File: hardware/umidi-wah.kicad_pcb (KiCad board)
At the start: 2 copper layers, 128 x 101 mm, 92 parts, among them J1 Power, J10 Midi_thru, J11 Midi_t/o, J12 Midi_out, J2 Pots Main, J3 Pots Front, J4 Switch, J5 Input, J6 Output, J7 Conn_02x05_Odd_Even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

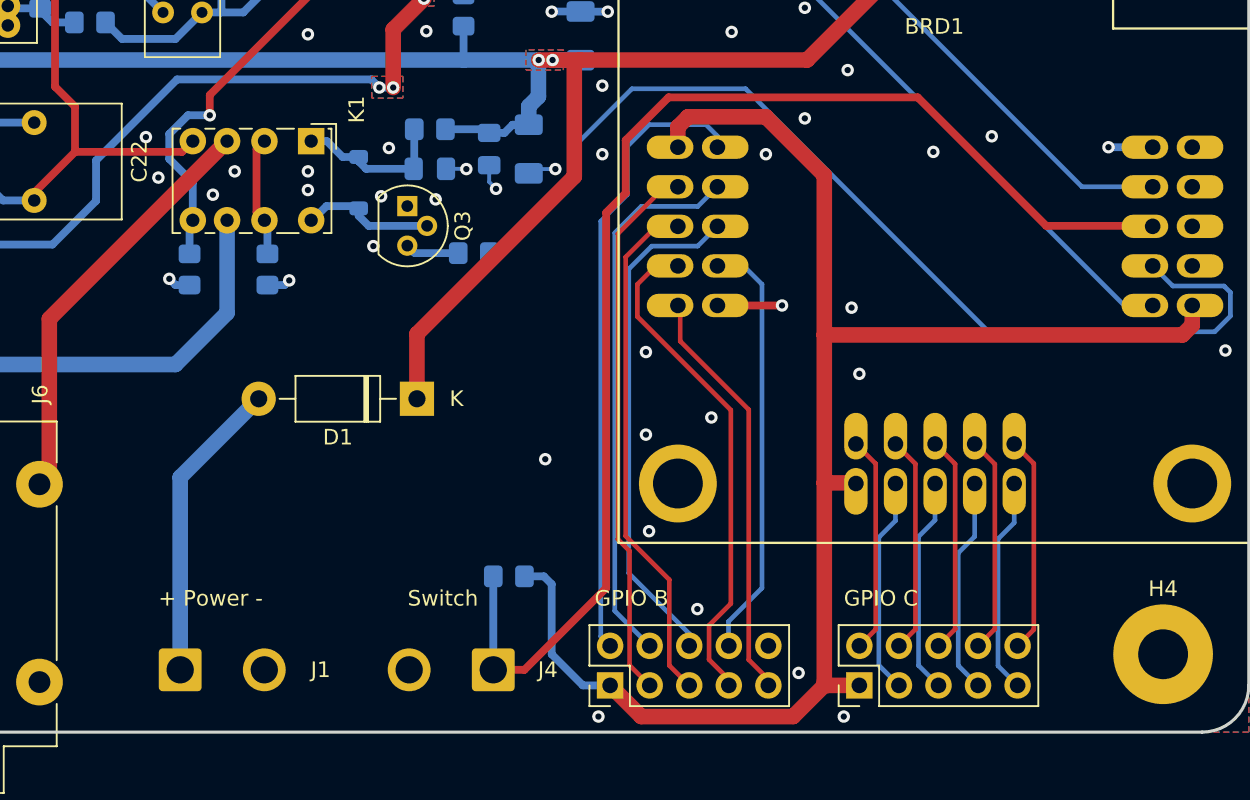
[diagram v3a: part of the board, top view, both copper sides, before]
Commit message: Rotate pwr connector (increase clearance to signal out)
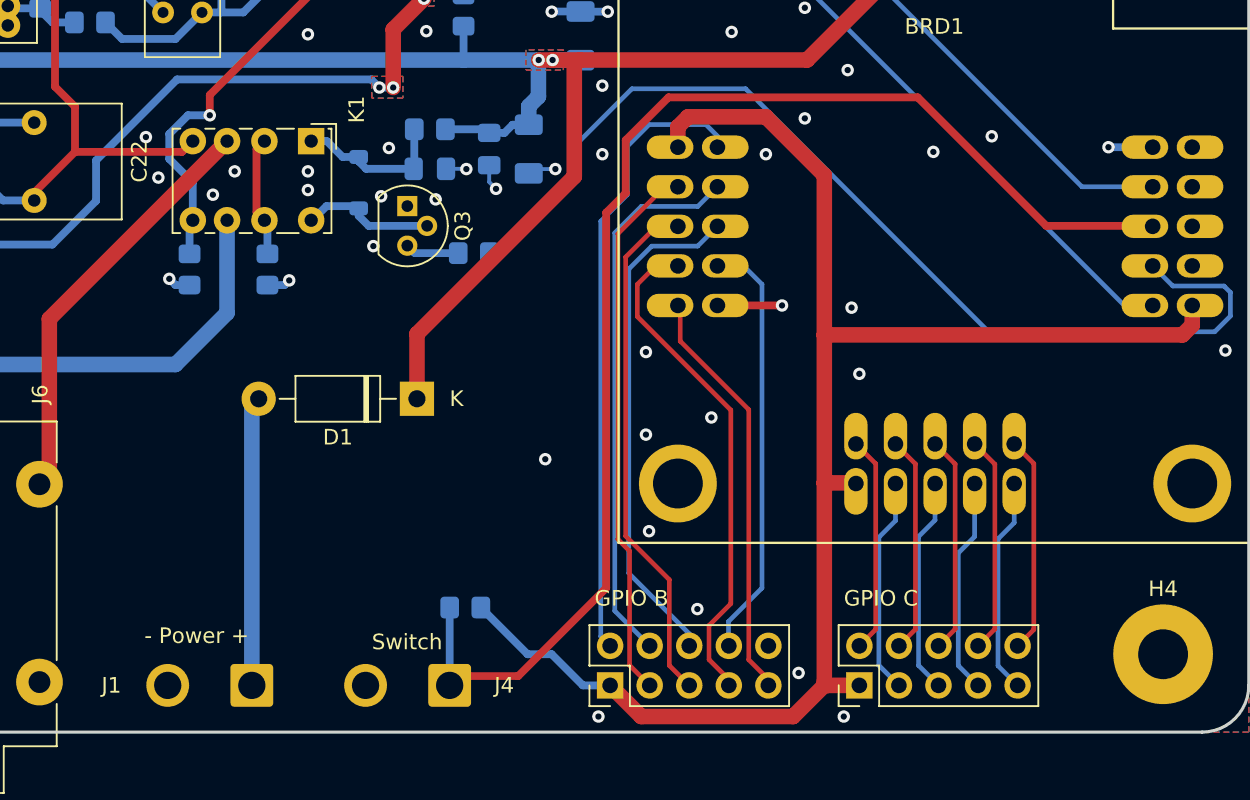
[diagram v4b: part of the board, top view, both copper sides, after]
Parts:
- moved J1 4.71 mm to (127.0, 134.0), turned to 180 degrees
- moved R25 3.44 mm to (140.7, 129.0)
- moved J4 2.97 mm to (139.7, 134.0)
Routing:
- net /toggle_switch: track 81.9 -> 85.3 mm
- net Net-(D1-A): track 19.5 -> 18.6 mm
- net /umidi_3v3: track 101.3 -> 100.6 mm
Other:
- board text added: "- Power +"
- board text added: "- pwr +"
- board text removed: "+ Power -"
- board text removed: "+ pwr -"
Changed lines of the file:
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@@
 	(footprint "Connector_Wire:SolderWire-1sqmm_1x02_P5.4mm_D1.4mm_OD2.7mm"
 		(layer "F.Cu")
-		(at 122.4 133)
+		(at 127 134 180)
 		(descr "Soldered wire connection, for 2 times 1 mm² wires, basic insulation, conductor diameter 1.4mm, outer diameter 2.7mm, size source Multi-Contact FLEXI-E 1.0 (https://ec.staubli.com/AcroFiles/Catalogues/TM_Cab-Main-11014119_(en)_hi.pdf), bend radius 3 times outer diameter, generated with kicad-footprint-generator")
 		(tags "connector wire 1sqmm")
 		(property "Reference" "J1"
-			(at 9.017 0 0)
+			(at 9.017 0 180)
 			(layer "F.SilkS")
 			(effects
@@
 		)
 		(property "Value" "Power"
-			(at 10.795 0 0)
+			(at 10.795 0 180)
 			(layer "F.Fab")
 			(effects
@@
 		)
 		(property "Footprint" ""
-			(at 0 0 0)
+			(at 0 0 180)
 			(unlocked yes)
 			(layer "F.Fab")
@@
 		)
 		(property "Datasheet" ""
-			(at 0 0 0)
+			(at 0 0 180)
 			(unlocked yes)
 			(layer "F.Fab")
@@
 		)
 		(property "Description" "Generic connector, single row, 01x02, script generated (kicad-library-utils/schlib/autogen/connector/)"
-			(at 0 0 0)
+			(at 0 0 180)
 			(unlocked yes)
 			(layer "F.Fab")
@@
 		)
 		(property "Supplier Link" ""
-			(at 0 0 0)
+			(at 0 0 180)
 			(layer "F.Fab")
 			(hide yes)
@@
 		(attr exclude_from_pos_files)
 		(fp_line
-			(start -2.1 -1.88)
-			(end -2.1 1.88)
+			(start 7.5 1.88)
+			(end 7.5 -1.88)
 			(stroke
 				(width 0.05)
@@
 		)
 		(fp_line
-			(start -2.1 1.88)
-			(end 2.1 1.88)
+			(start 7.5 -1.88)
+			(end 3.3 -1.88)
 			(stroke
 				(width 0.05)
@@
 		)
 		(fp_line
-			(start 2.1 -1.88)
-			(end -2.1 -1.88)
+			(start 3.3 1.88)
+			(end 7.5 1.88)
 			(stroke
 				(width 0.05)
@@
 		)
 		(fp_line
-			(start 2.1 1.88)
-			(end 2.1 -1.88)
+			(start 3.3 -1.88)
+			(end 3.3 1.88)
 			(stroke
 				(width 0.05)
@@
 		)
 		(fp_line
-			(start 3.3 -1.88)
-			(end 3.3 1.88)
+			(start 2.1 1.88)
+			(end 2.1 -1.88)
 			(stroke
 				(width 0.05)
@@
 		)
 		(fp_line
-			(start 3.3 1.88)
-			(end 7.5 1.88)
+			(start 2.1 -1.88)
+			(end -2.1 -1.88)
 			(stroke
 				(width 0.05)
@@
 		)
 		(fp_line
-			(start 7.5 -1.88)
-			(end 3.3 -1.88)
+			(start -2.1 1.88)
+			(end 2.1 1.88)
 			(stroke
 				(width 0.05)
@@
 		)
 		(fp_line
-			(start 7.5 1.88)
-			(end 7.5 -1.88)
+			(start -2.1 -1.88)
+			(end -2.1 1.88)
 			(stroke
 				(width 0.05)
@@
 		)
 		(fp_circle
-			(center 0 0)
-			(end 1.35 0)
+			(center 5.4 0)
+			(end 6.75 0)
 			(stroke
 				(width 0.1)
@@
 		)
 		(fp_circle
-			(center 5.4 0)
-			(end 6.75 0)
+			(center 0 0)
+			(end 1.35 0)
 			(stroke
 				(width 0.1)
@@
 		)
 		(fp_text user "${REFERENCE}"
-			(at 2.7 0 90)
+			(at 2.7 0 270)
 			(layer "F.Fab")
 			(effects
@@
 		)
 		(pad "1" thru_hole roundrect
-			(at 0 0)
+			(at 0 0 180)
 			(size 2.75 2.75)
 			(drill 1.75)
@@
 		)
 		(pad "2" thru_hole circle
-			(at 5.4 0)
+			(at 5.4 0 180)
 			(size 2.75 2.75)
 			(drill 1.75)
@@
 	(footprint "Connector_Wire:SolderWire-1sqmm_1x02_P5.4mm_D1.4mm_OD2.7mm"
 		(layer "F.Cu")
-		(at 142.5 133 180)
+		(at 139.7 134 180)
 		(descr "Soldered wire connection, for 2 times 1 mm² wires, basic insulation, conductor diameter 1.4mm, outer diameter 2.7mm, size source Multi-Contact FLEXI-E 1.0 (https://ec.staubli.com/AcroFiles/Catalogues/TM_Cab-Main-11014119_(en)_hi.pdf), bend radius 3 times outer diameter, generated with kicad-footprint-generator")
 		(tags "connector wire 1sqmm")
@@
 	(footprint "Resistor_SMD:R_0805_2012Metric_Pad1.20x1.40mm_HandSolder"
 		(layer "B.Cu")
-		(at 143.5 127)
+		(at 140.7 129)
 		(descr "Resistor SMD 0805 (2012 Metric), square (rectangular) end terminal, IPC_7351 nominal with elongated pad for handsoldering. (Body size source: IPC-SM-782 page 72, https://www.pcb-3d.com/wordpress/wp-content/uploads/ipc-sm-782a_amendment_1_and_2.pdf), generated with kicad-footprint-generator")
 		(tags "resistor handsolder")
@@
 		)
 	)
-	(gr_text "+ Power -"
-		(at 121 129 0)
+	(gr_text "- Power +"
+		(at 120.1 131.4 0)
 		(layer "F.SilkS")
 		(effects
@@
 	)
 	(gr_text "Switch"
-		(at 137 129 0)
+		(at 134.7 131.8 0)
 		(layer "F.SilkS")
 		(effects
@@
 	)
 	(gr_text "sw"
-		(at 138 128 0)
+		(at 135.5 131 0)
 		(layer "F.Mask")
 		(effects
 			(font
-				(size 1.5 1.5)
+				(size 1.2 1.2)
 				(thickness 0.3)
 				(bold yes)
@@
 		)
 	)
-	(gr_text "+ pwr -"
-		(at 120 128 0)
+	(gr_text "- pwr +"
+		(at 120.15779 131 0)
 		(layer "F.Mask")
 		(effects
 			(font
-				(size 1.5 1.5)
+				(size 1.2 1.2)
 				(thickness 0.3)
 				(bold yes)
@@
 	)
 	(segment
-		(start 122.4 120.64)
-		(end 127.44 115.6)
+		(start 127 134)
+		(end 127 116.04)
 		(width 1)
 		(layer "B.Cu")
@@
 	)
 	(segment
-		(start 122.4 133)
-		(end 122.4 120.64)
+		(start 127 116.04)
+		(end 127.44 115.6)
 		(width 1)
 		(layer "B.Cu")
@@
 	)
 	(segment
-		(start 146.25 127.5)
+		(start 144.7 132)
 		(end 146.25 132)
 		(width 0.5)
@@
 	)
 	(segment
-		(start 148.25 134)
-		(end 150 134)
-		(width 0.5)
-		(layer "B.Cu")
-		(net 25)
-	)
-	(segment
-		(start 144.5 127)
-		(end 145.75 127)
+		(start 146.25 132)
+		(end 148.25 134)
 		(width 0.5)
 		(layer "B.Cu")
@@
 	)
 	(segment
-		(start 146.25 132)
-		(end 148.25 134)
+		(start 148.25 134)
+		(end 150 134)
 		(width 0.5)
 		(layer "B.Cu")
@@
 	)
 	(segment
-		(start 145.75 127)
-		(end 146.25 127.5)
+		(start 141.7 129)
+		(end 144.7 132)
 		(width 0.5)
 		(layer "B.Cu")
@@
 	)
 	(segment
-		(start 153.75 96.25)
-		(end 169.75 96.25)
+		(start 151 102.4)
+		(end 149.75 103.65)
 		(width 0.5)
 		(layer "F.Cu")
@@
 	)
 	(segment
-		(start 178 104.5)
-		(end 184.8 104.5)
+		(start 169.75 96.25)
+		(end 153.75 96.25)
 		(width 0.5)
 		(layer "F.Cu")
@@
 	)
 	(segment
-		(start 149.75 127.75)
-		(end 149.75 103.65)
+		(start 184.8 104.5)
+		(end 178 104.5)
 		(width 0.5)
 		(layer "F.Cu")
@@
 	)
 	(segment
-		(start 144.5 133)
-		(end 149.75 127.75)
+		(start 151 99)
+		(end 151 102.4)
 		(width 0.5)
 		(layer "F.Cu")
@@
 	)
 	(segment
-		(start 169.75 96.25)
-		(end 178 104.5)
+		(start 144.1 133.4)
+		(end 140.3 133.4)
 		(width 0.5)
 		(layer "F.Cu")
@@
 	)
 	(segment
-		(start 149.75 103.65)
-		(end 151 102.4)
+		(start 178 104.5)
+		(end 169.75 96.25)
 		(width 0.5)
 		(layer "F.Cu")
@@
 	)
 	(segment
-		(start 151 99)
-		(end 153.75 96.25)
+		(start 140.3 133.4)
+		(end 139.7 134)
 		(width 0.5)
 		(layer "F.Cu")
@@
 	)
 	(segment
-		(start 151 102.4)
+		(start 153.75 96.25)
 		(end 151 99)
 		(width 0.5)
@@
 	)
 	(segment
-		(start 143.7 133)
-		(end 144.5 133)
+		(start 149.75 103.65)
+		(end 149.75 127.75)
+		(width 0.5)
+		(layer "F.Cu")
+		(net 28)
+	)
+	(segment
+		(start 149.75 127.75)
+		(end 144.1 133.4)
 		(width 0.5)
 		(layer "F.Cu")
@@
 	)
 	(segment
-		(start 142.5 127)
-		(end 142.5 133)
+		(start 139.7 129)
+		(end 139.7 134)
 		(width 0.5)
 		(layer "B.Cu")

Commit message: Replace gpio connectors by boxed headers
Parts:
- J7, J8: footprint Connector_PinHeader_2.54mm:PinHeader_2x05_P2.54mm_Vertical -> Connector_IDC:IDC-Header_2x05_P2.54mm_Vertical
- moved J4 14.1 mm to (129.4, 124.2)
- moved R25 7.23 mm to (135.2, 124.2)
- moved J7 7.07 mm to (143.0, 133.0)
- moved J1 3.00 mm to (130.0, 134.0)
- moved J8 1.41 mm to (165.0, 133.0)
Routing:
- net /umidi_3v3: track 100.6 -> 108.3 mm
- net Net-(BRD1B-PA6(ADC6)): track 27.5 -> 31.2 mm
- net Net-(BRD1B-PA5(ADC5)): track 32.4 -> 35.0 mm
- net Net-(BRD1B-PA7(ADC7)): track 26.8 -> 28.6 mm
- net Net-(BRD1B-PA3(ADC3)): track 33.4 -> 31.9 mm
- net Net-(D1-A): track 18.6 -> 20.0 mm
- net Net-(BRD1B-PA0(ADC0)): track 40.4 -> 41.8 mm
- net Net-(BRD1B-PA4(ADC4)): track 32.6 -> 31.3 mm
- net /toggle_switch: track 85.3 -> 84.2 mm, vias 0 -> 1
- net Net-(BRD1C-PB1): track 13.9 -> 13.3 mm
- net Net-(BRD1C-PC1(SCL)): track 13.9 -> 13.3 mm
- net Net-(BRD1C-PB3(DACB::DAC1)): track 13.9 -> 13.3 mm
- net Net-(BRD1C-PB2(DACB::DAC0)): track 13.9 -> 13.3 mm
- net Net-(BRD1C-PC3(C0::TXD0)): track 13.9 -> 13.3 mm
- net Net-(BRD1C-PC2(C0::RXD0)): track 13.9 -> 13.4 mm
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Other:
- board text added: "gpio1"
- board text added: "gpio2"
- board text removed: "- Power +"
- board text removed: "Switch"

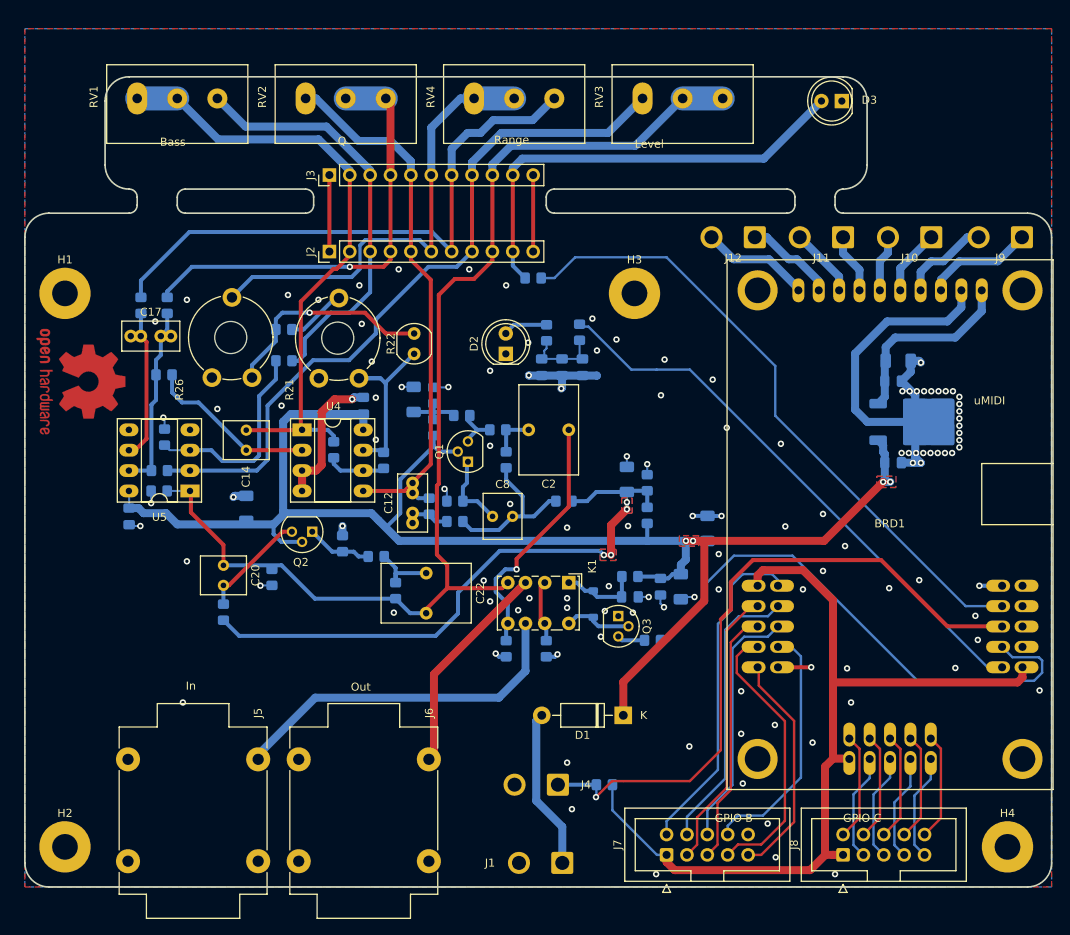
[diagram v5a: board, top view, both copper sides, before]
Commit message: Small tweaks -> DRC clean
Fix typo in board name, move umidi slighty south
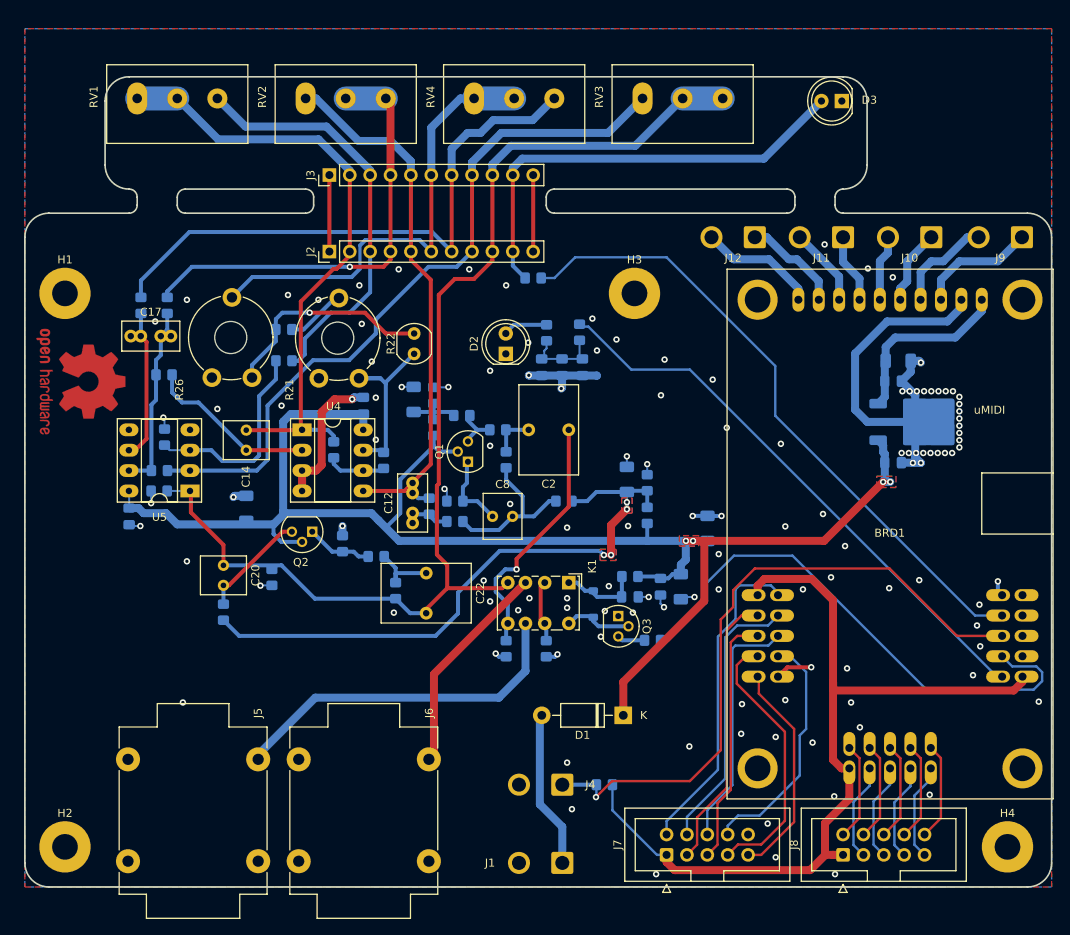
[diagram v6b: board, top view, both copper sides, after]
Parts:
- moved BRD1 1.17 mm to (170.9, 93.0)
- moved J4 0.55 mm to (130.0, 124.2)
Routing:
- net GND: track 147.4 -> 144.7 mm, vias 118 -> 125
- net Net-(BRD1B-PA0(ADC0)): track 41.8 -> 40.3 mm
- net Net-(BRD1C-PC2(C0::RXD0)): track 13.4 -> 12.2 mm
- net Net-(BRD1C-PB2(DACB::DAC0)): track 13.3 -> 12.2 mm
- net Net-(BRD1C-PB0): track 13.3 -> 12.2 mm
- net Net-(BRD1B-PA7(ADC7)): track 28.6 -> 27.4 mm
- net Net-(BRD1A-MIDI_thru+): track 8.22 -> 9.39 mm
- net Net-(BRD1A-MIDI_out-): track 13.7 -> 14.9 mm
- net Net-(BRD1A-MIDI_out+): track 11.4 -> 12.6 mm
- net Net-(BRD1A-MIDI_in-): track 11.3 -> 12.5 mm
- net Net-(BRD1A-MIDI_in+): track 13.6 -> 14.8 mm
- net Net-(BRD1A-MIDI_T/O-): track 8.65 -> 9.82 mm
- net Net-(BRD1A-MIDI_T/O+): track 7.47 -> 8.64 mm
- net Net-(BRD1A-5..9V): track 23.9 -> 22.7 mm
- net Net-(BRD1A-MIDI_thru-): track 7.04 -> 8.21 mm
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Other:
- board text added: "umidi-wah 0.5 {dblquote}demon{dblquote} [2024]"
- board text removed: "GPIO B"
- board text removed: "GPIO C"
- board text removed: "In"
- board text removed: "Out"
- board text removed: "umidi-wah 0.5 {dblquote}daemon{dblquote} [2024]"
